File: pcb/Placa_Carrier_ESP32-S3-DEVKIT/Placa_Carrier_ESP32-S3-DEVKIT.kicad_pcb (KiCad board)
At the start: 2 copper layers, 150 x 45.5 mm, 45 parts, among them J1 12V IN, J2 AN_IN, J3 RELE, J4 CAN, J5 DevKit_J1, J6 DevKit_J3, J7 EXP_J1, J8 EXP_J3, K1 SRD-05VDC, Q1 BC817, SW1 SW_Push, SW2 SW_Push, U1 AMS1117-ADJ, U3 MCP2562-E-SN

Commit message: Actualiza ruteo
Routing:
- net /REL_COM: track 0.00 -> 30.2 mm
- net /REL_NC: track 0.00 -> 14.3 mm
- net /REL_NA: track 0.00 -> 11.5 mm
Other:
- board size 150 x 45.5 mm -> 152.3 x 45.5 mm
- board text added: "220 V AC"
- board text removed: "220 V"
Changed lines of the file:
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@@
 		)
 		(property "Value" "RELE"
-			(at 5.08 5.66 90)
+			(at 15.2 -5 90)
 			(layer "F.Fab")
 			(effects
@@
 	(gr_rect
 		(start 100 60)
-		(end 250 105.5)
+		(end 252.3 105.5)
 		(stroke
 			(width 0.1)
@@
 		)
 	)
-	(gr_text "1-COM 2-NA 3-NC"
-		(at 241 84.6 0)
-		(layer "F.SilkS")
-		(effects
-			(font
-				(size 1 1)
-				(thickness 0.15)
-			)
-		)
-	)
 	(gr_text "ANTENA: sin cobre"
 		(at 171.5 82.6 90)
@@
 		)
 	)
+	(gr_text "1-COM 2-NA 3-NC"
+		(at 250.9 75.5 90)
+		(layer "F.SilkS")
+		(effects
+			(font
+				(size 1 1)
+				(thickness 0.15)
+			)
+		)
+	)
 	(gr_text "PLACA CARRIER ESP32-S3-DevKitC-1  Rev A"
 		(at 136 82.6 0)
@@
 		)
 	)
-	(gr_text "220 V"
+	(gr_text "220 V AC"
 		(at 226 82.6 0)
 		(layer "F.SilkS")
@@
 		(net "/+5V_REG")
 	)
+	(segment
+		(start 221.5 69)
+		(end 232.9 80.4)
+		(width 2)
+		(layer "F.Cu")
+		(net "/REL_COM")
+	)
+	(segment
+		(start 232.9 80.4)
+		(end 244.5 80.4)
+		(width 2)
+		(layer "F.Cu")
+		(net "/REL_COM")
+	)
+	(segment
+		(start 219 69)
+		(end 221.5 69)
+		(width 2)
+		(layer "F.Cu")
+		(net "/REL_COM")
+	)
+	(segment
+		(start 244.23 75.05)
+		(end 244.5 75.32)
+		(width 0.2)
+		(layer "F.Cu")
+		(net "/REL_NA")
+	)
+	(segment
+		(start 233.15 75.05)
+		(end 244.23 75.05)
+		(width 2)
+		(layer "F.Cu")
+		(net "/REL_NA")
+	)
+	(segment
+		(start 233.2 63)
+		(end 240.44 70.24)
+		(width 2)
+		(layer "F.Cu")
+		(net "/REL_NC")
+	)
+	(segment
+		(start 240.44 70.24)
+		(end 244.5 70.24)
+		(width 2)
+		(layer "F.Cu")
+		(net "/REL_NC")
+	)
 	(zone
 		(layers "F.Cu" "B.Cu")
@@
 		(polygon
 			(pts
-				(xy 100.5 60.5) (xy 249.5 60.5) (xy 249.5 105) (xy 100.5 105)
-			)
-		)
+				(xy 100.5 60.5) (xy 251.7 60.5) (xy 251.7 105) (xy 100.5 105)
+			)
+		)

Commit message: actualiza ruteo con par diferencial
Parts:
- moved R1 4.21 mm to (234.0, 89.2), turned to -90 degrees
- moved C4 4.10 mm to (231.6, 93.4), turned to 0 degrees
- moved JP1 4.03 mm to (238.0, 88.0)
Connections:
- net /CANH renamed /CAN_P
- net /CANL renamed /CAN_N
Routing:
- net /CAN_N: track 0.00 -> 25.6 mm
- net /CAN_P: track 0.00 -> 23.0 mm
- net Net-(JP1-B): track 0.00 -> 4.08 mm

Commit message: Actualiza PCB
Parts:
- U3: value MCP2562-E-SN -> MCP2562
- moved R6 17.0 mm to (199.9, 92.6), turned to 90 degrees
- moved C5 5.66 mm to (195.6, 88.7)
- moved D5 5.50 mm to (186.5, 91.9)
- moved R7 4.53 mm to (186.5, 88.5), turned to 180 degrees
- moved D6 4.21 mm to (194.5, 91.9)
- moved J4 3.12 mm to (226.4, 99.7)
- moved C4 2.38 mm to (233.9, 92.8)
- moved C3 1.33 mm to (222.8, 89.2)
- moved C6 1.30 mm to (186.6, 82.1)
- moved J2 0.62 mm to (184.1, 99.7)
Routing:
- net /CAN_P: track 23.0 -> 19.2 mm
- net +3V3: track 0.00 -> 3.42 mm
- net /CAN_N: track 25.6 -> 24.0 mm
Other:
- board size 152.3 x 45.5 mm -> 152.3 x 50 mm

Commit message: Actualiza ruteo
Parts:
- moved SW2 3.38 mm to (206.6, 98.7)
- moved R5 3.20 mm to (216.6, 100.7)
- moved SW1 1.23 mm to (206.6, 87.5)
- moved R4 0.56 mm to (216.6, 89.5)
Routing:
- net /VIN: track 0.00 -> 38.7 mm
- net Net-(D7-K): track 0.00 -> 29.9 mm
- net +5V: track 0.00 -> 27.5 mm
- net /AN1: track 0.00 -> 22.3 mm
- net +3V3: track 3.42 -> 25.3 mm
- net /+5V_REG: track 0.00 -> 16.9 mm
- net Net-(Q1-B): track 0.00 -> 14.9 mm
- net Net-(J2-Pin_2): track 0.00 -> 13.7 mm
- net Net-(U1-ADJ): track 0.00 -> 11.0 mm
- net /+12V_IN: track 0.00 -> 5.75 mm
- net GND: track 0.00 -> 5.62 mm
- net /SW2: track 0.00 -> 5.50 mm
- net /SW1: track 0.00 -> 5.50 mm

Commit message: actualiza ruteo
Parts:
- JP1: value TERM_CAN -> TERM.
- moved H4 2.62 mm to (248.2, 104.0)
- moved H3 2.41 mm to (248.1, 61.7)
- moved H1 1.90 mm to (103.6, 61.6)
- moved H2 1.81 mm to (103.7, 103.8)
- moved D3 0.73 mm to (212.7, 75.4), turned to 180 degrees
- moved D7 0.73 mm to (212.7, 81.8), turned to 180 degrees
- moved R10 0.73 mm to (207.5, 81.8)
- moved R2 0.73 mm to (207.5, 75.4)
- moved D4 0.73 mm to (212.7, 78.6), turned to 180 degrees
- moved R3 0.73 mm to (207.5, 78.6)
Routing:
- net Net-(D7-K): track 29.9 -> 41.4 mm
- net /SW2: track 5.50 -> 12.0 mm
- net /SW1: track 5.50 -> 12.0 mm
- net Net-(D7-A): track 0.00 -> 2.16 mm
- net Net-(D4-A): track 0.00 -> 2.16 mm
- net Net-(D3-A): track 0.00 -> 2.16 mm
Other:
- board text added: "EIE-FCEIA-UNR"
- board text added: "dsi"

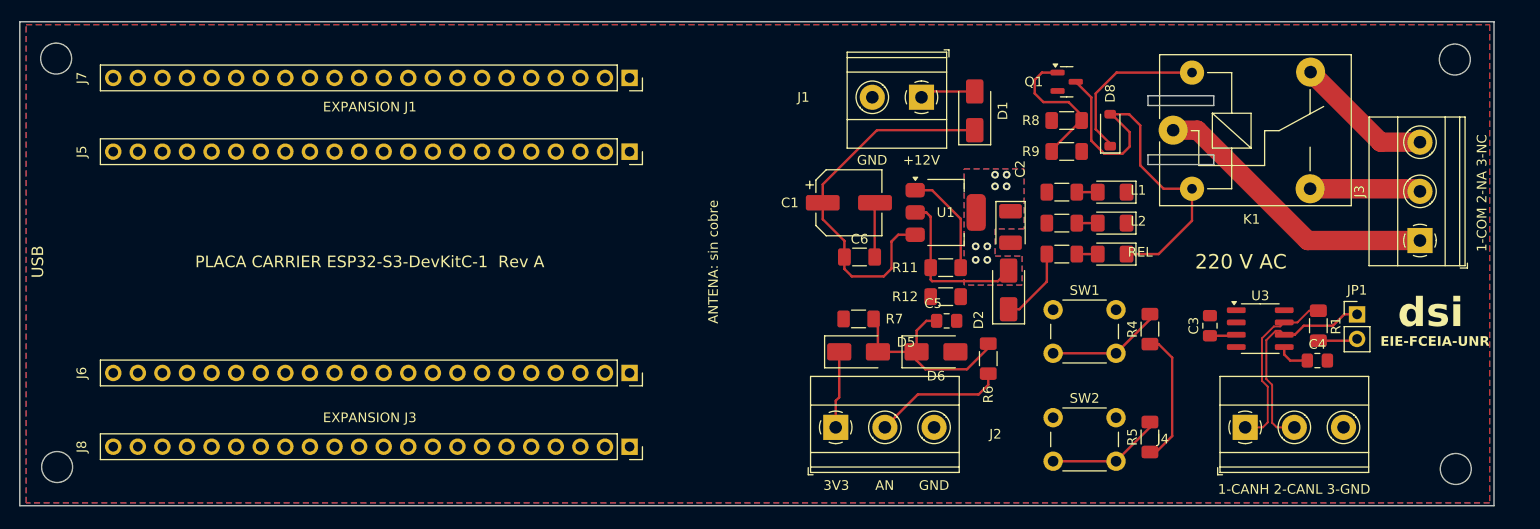
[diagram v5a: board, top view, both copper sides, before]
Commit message: Empieza a cambiar hoja a A4
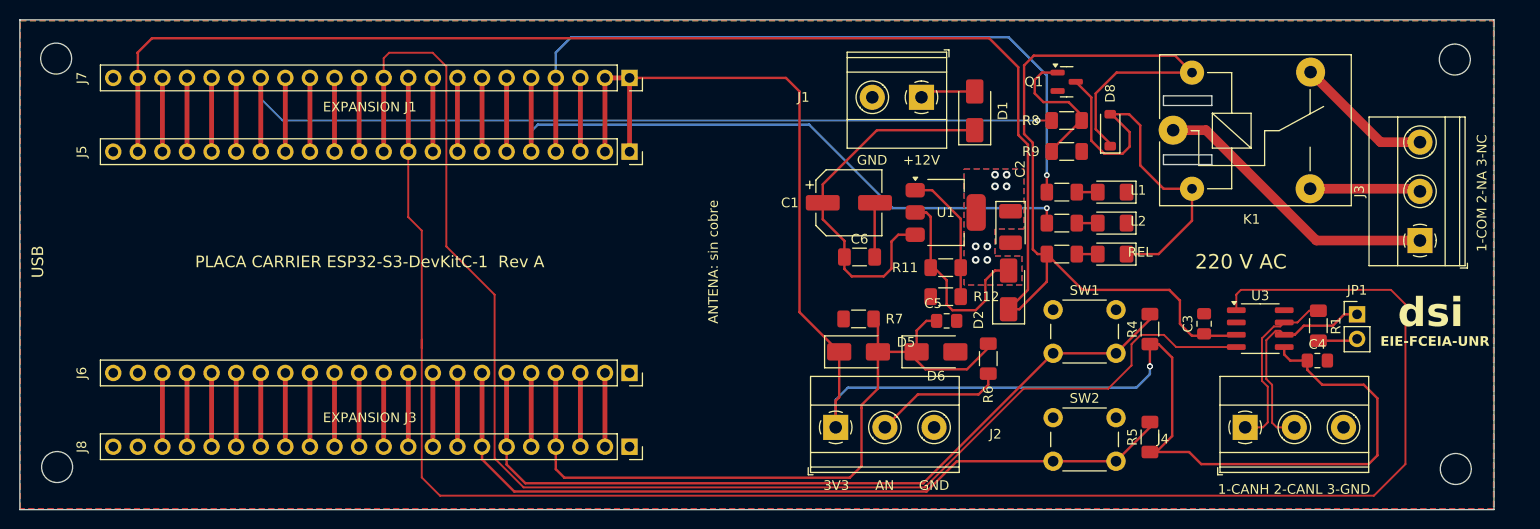
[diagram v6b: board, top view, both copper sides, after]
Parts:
- JP1: value TERM. -> TERM_CAN
- U3: value MCP2562 -> MCP2562-E-SN
- moved C3 0.63 mm to (222.2, 89.0)
- turned R12 to 180 degrees
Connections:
- J5 pad 7: /SW1 -> /GPIO7
- J5 pad 8: /SW2 -> /GPIO15
- J6 pad 6: /GPIO42 -> /SW1
- J6 pad 7: /GPIO41 -> /SW2
- J7 pad 7: /SW1 -> /GPIO7
- J7 pad 8: /SW2 -> /GPIO15
- J8 pad 6: /GPIO42 -> /SW1
- J8 pad 7: /GPIO41 -> /SW2
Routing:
- net +5V: track 27.7 -> 218.3 mm
- net /CAN_TX: track 0.00 -> 182.9 mm
- net /CAN_RX: track 0.00 -> 145.9 mm
- net +3V3: track 25.3 -> 169.1 mm, vias 0 -> 2
- net /REL1: track 0.00 -> 92.4 mm, vias 0 -> 1
- net /LED1: track 0.00 -> 75.4 mm, vias 0 -> 1
- net /SW1: track 12.0 -> 84.3 mm
- net /SW2: track 12.0 -> 82.6 mm
- net /LED2: track 0.00 -> 68.5 mm, vias 0 -> 1
- net /AN1: track 22.3 -> 77.2 mm
- net /RST: track 0.00 -> 7.62 mm
- net /GPIO9: track 0.00 -> 7.62 mm
- net /GPIO8: track 0.00 -> 7.62 mm
- net /GPIO7: track 0.00 -> 7.62 mm
- net /GPIO6: track 0.00 -> 7.62 mm
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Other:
- board size 152.3 x 50 mm -> 152.3 x 50.6 mm

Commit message: Sube PCB ruteado sin refinar
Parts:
- moved H2 0.50 mm to (103.4, 104.2)
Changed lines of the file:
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@@
 	(footprint "MountingHole:MountingHole_3.2mm_M3"
 		(layer "F.Cu")
-		(at 103.7 103.8)
+		(at 103.4 104.2)
 		(descr "Mounting Hole 3.2mm, no annular, M3")
 		(tags "mounting hole 3.2mm no annular m3")

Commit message: Actualiza PCB
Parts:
- moved H2 0.45 mm to (103.8, 104.2)
- moved R4 0.40 mm to (217.0, 89.5)
- moved R5 0.40 mm to (217.0, 100.7)
- moved H1 0.25 mm to (103.8, 61.6)
- moved H4 0.21 mm to (248.2, 104.2)
- moved H3 0.11 mm to (248.2, 61.6)
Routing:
- net GND: track 5.62 -> 23.8 mm, vias 0 -> 12
- net Net-(D7-K): track 41.4 -> 36.3 mm
- net /REL_COM: track 30.2 -> 34.6 mm
- net +3V3: vias 2 -> 1
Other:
- board text added: "0"
- board text added: "11"
- board text added: "12"
- board text added: "13"
- board text added: "14"
- board text added: "15"
- board text added: "16"
- board text added: "19"
- board text added: "2"
- board text added: "20"
- board text added: "21"
- board text added: "3"
- board text added: "35"
- board text added: "36"
- board text added: "37"
- board text added: "38"
- board text added: "39"
- board text added: "40"
- board text added: "45"
- board text added: "46"
- board text added: "47"
- board text added: "48"
- board text added: "5V"
- board text added: "6"
- board text added: "7"
- board text added: "8"
- board text added: "9"
- board text added: "AN1"
- board text added: "Autor: Prof. Ing. Daniel Márquez"
- board text added: "CANH CANL GND"
- board text added: "COM NA NC"
- board text added: "CRX"
- board text added: "CTX"
- board text added: "LD1"
- board text added: "LD2"
- board text added: "RST"
- board text added: "RX0"
- board text added: "SW1"
- board text added: "SW2"
- board text added: "TX0"
- board text removed: "1-CANH 2-CANL 3-GND"
- board text removed: "1-COM 2-NA 3-NC"
- board text removed: "EXPANSION J1"
- board text removed: "EXPANSION J3"
- board text removed: "L1"
- board text removed: "L2"
